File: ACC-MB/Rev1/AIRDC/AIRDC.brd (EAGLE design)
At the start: 107 x 63 mm, 6 parts

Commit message: update
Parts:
- added LED1, LED2: (no value), ACC-MB-R0:LED3MM
- added R2, R4: (no value), ACC-MB-R0:R0805
- added X13: 5566-4, ACC-MB-R0:5566-4
- moved D1 10.0 mm to (-2.00, 45.0)
- moved R1 9.06 mm to (-7.00, 40.0)
- moved C1 2.24 mm to (-9.00, 59.0)
- flipped U$2 to the top
- flipped U$3 to the top
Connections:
- new net N$1: LED2.K, R2.2
- new net N$5: LED1.K, R4.2
- net AUX_A1: now also U$2.10, U$2.4, U$2.5, U$2.9, X13.1, X13.2; no longer U$2.1, U$2.2, U$2.6, U$2.7
- net AUX_A2: now also U$2.1, U$2.2, U$2.6, U$2.7, X13.3, X13.4; no longer U$2.10, U$2.4, U$2.5, U$2.9
- net COIL_X1: now also LED1.A
- net COIL_X2: now also LED2.A
- net GND: now also R2.1, R4.1
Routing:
- net AUX_A1: track 73.1 -> 114.5 mm
- net AUX_A2: track 59.1 -> 92.5 mm
- net AUX_T1: track 53.7 -> 82.0 mm
- net COIL_X2: track 70.5 -> 87.5 mm
- net AUX_T2: track 83.9 -> 96.1 mm
- net N$1: track 0.00 -> 4.16 mm
- net N$3: track 20.9 -> 17.5 mm
- net N$5: track 0.00 -> 3.19 mm
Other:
- outline, holes or cut-outs redrawn

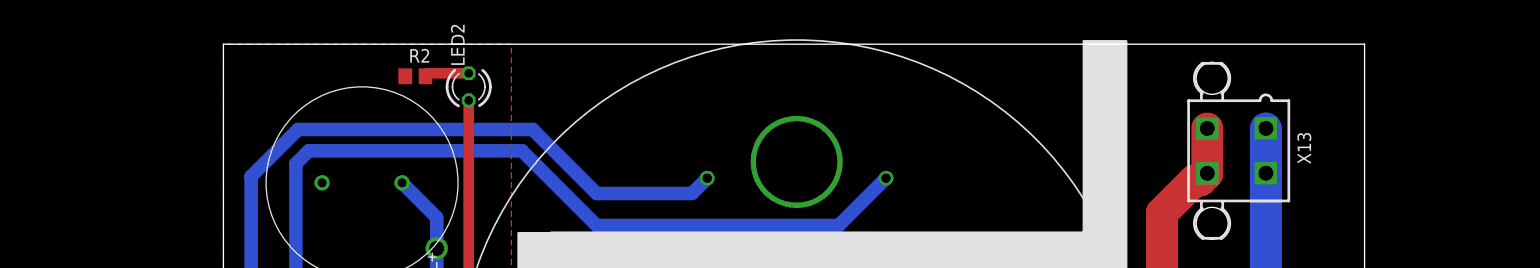
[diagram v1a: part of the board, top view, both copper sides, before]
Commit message: 7792 added to all DC
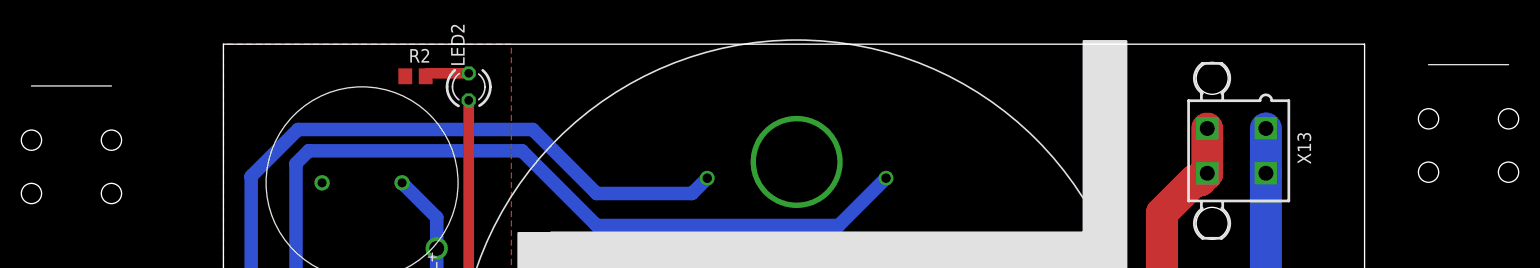
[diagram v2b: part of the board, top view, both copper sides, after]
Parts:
- added U$4, U$5: 7792, ACC-MB-R0:7792
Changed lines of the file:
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@@
 <attribute name="SPICEPREFIX" value="R" x="-4" y="69" size="1.778" layer="27" display="off"/>
 </element>
+<element name="U$4" library="ACC-MB-R0" library_urn="urn:adsk.eagle:library:13208985" package="7792" package3d_urn="urn:adsk.eagle:package:14511284/2" value="7792" x="-40" y="58"/>
+<element name="U$5" library="ACC-MB-R0" library_urn="urn:adsk.eagle:library:13208985" package="7792" package3d_urn="urn:adsk.eagle:package:14511284/2" value="7792" x="91" y="60"/>
 </elements>
 <signals>
